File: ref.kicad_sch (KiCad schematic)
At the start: 54 parts, among them Q201 Q_NPN_BCE, U201 Opamp_Dual, U202 ADR1000, U203 ADA4523-1

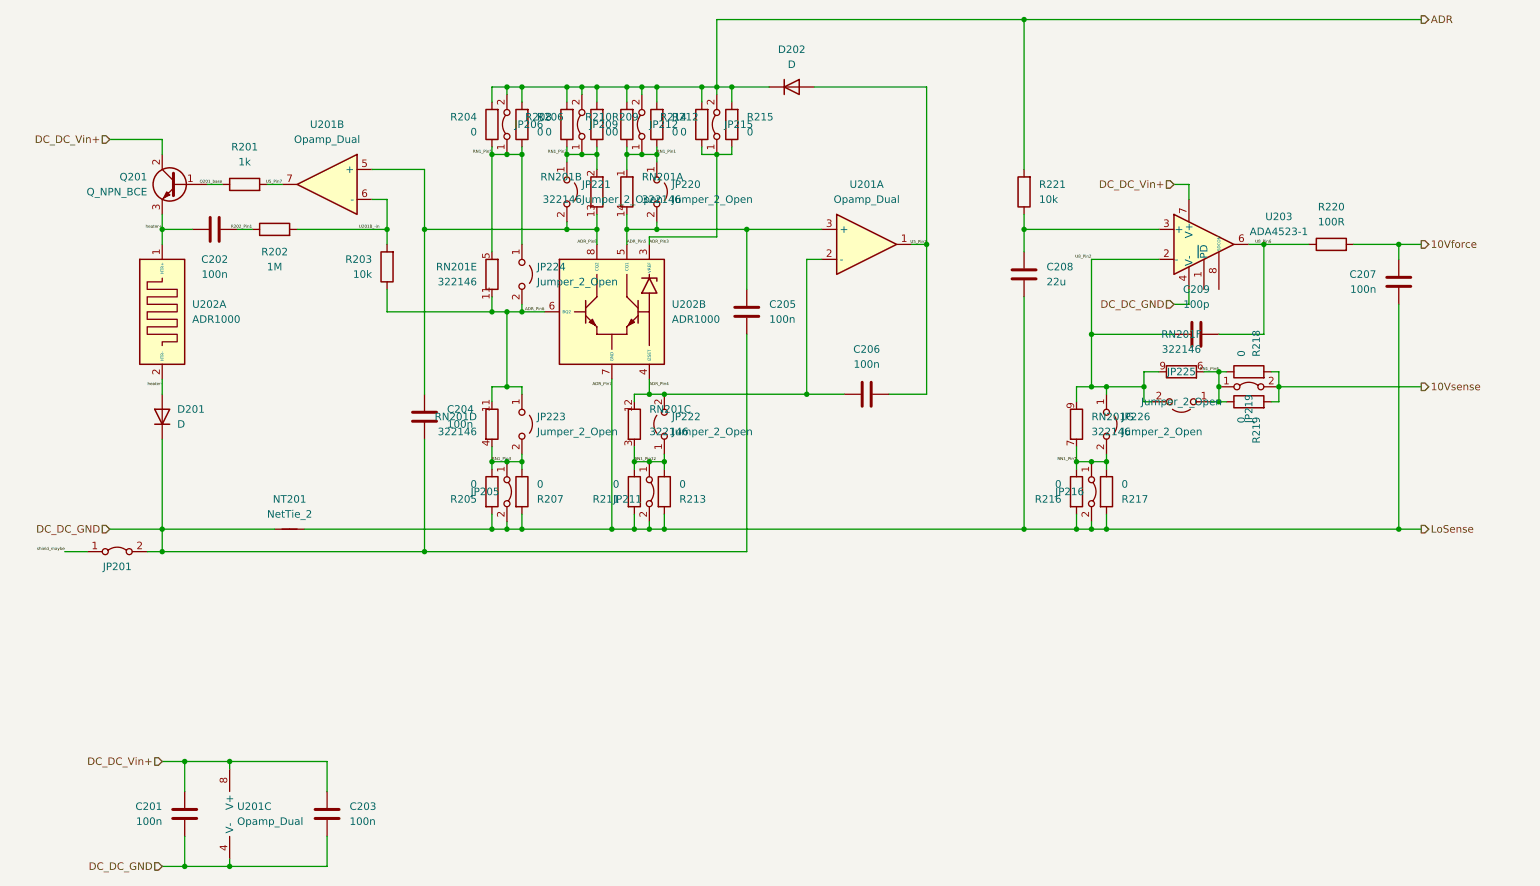
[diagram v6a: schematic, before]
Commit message: schematics updated to rev.2
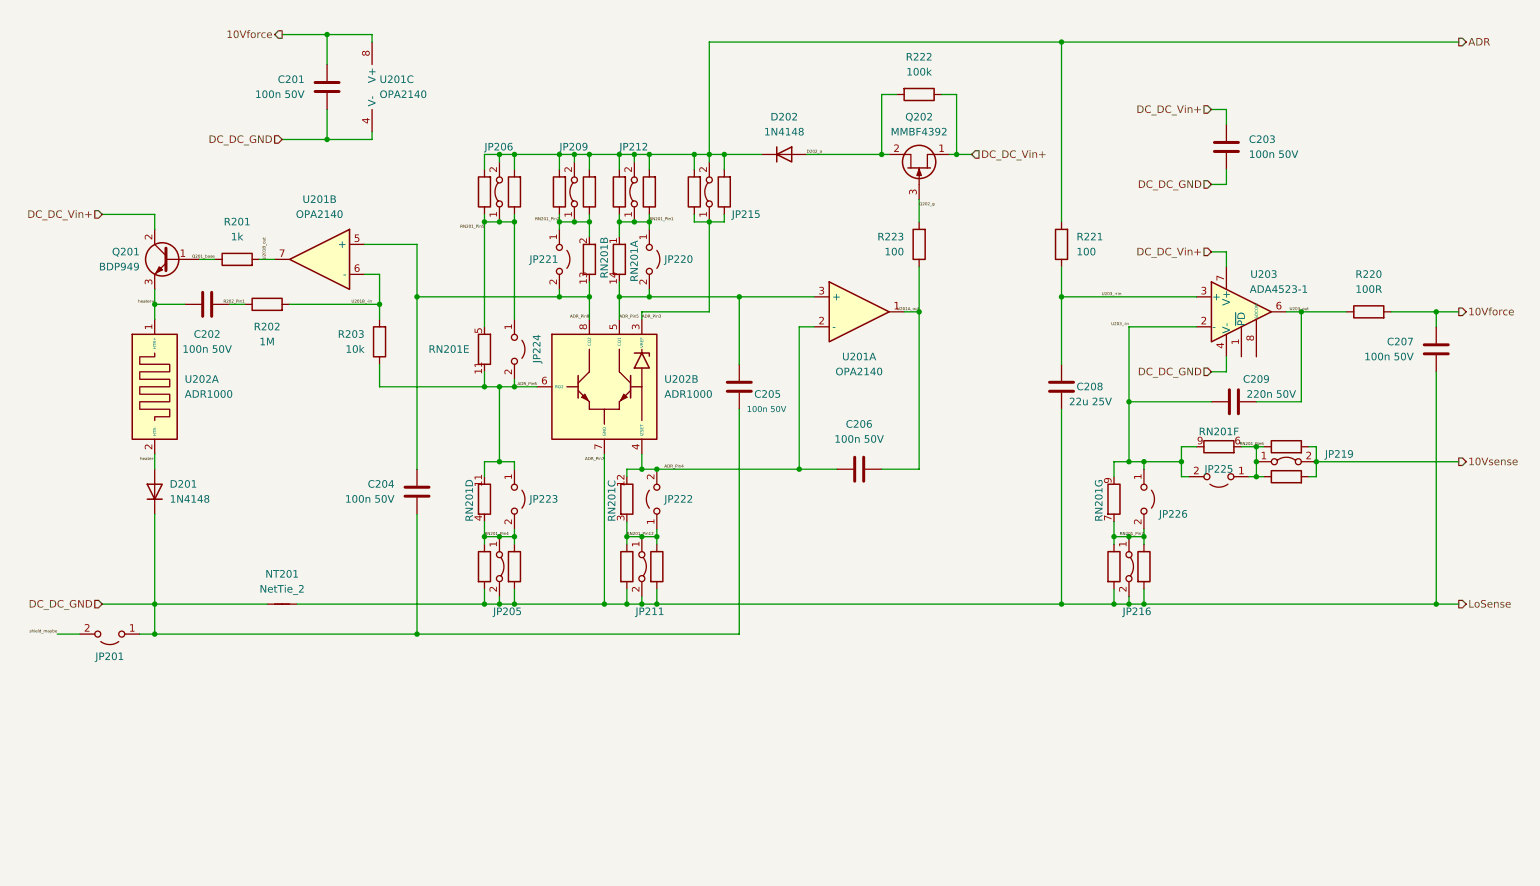
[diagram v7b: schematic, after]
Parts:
- removed JP201: Jumper_2_Bridged, Jumper:SolderJumper-2_P1.3mm_Bridged_RoundedPad1.0x1.5mm, symbol Jumper:Jumper_2_Bridged
- added JP201: Jumper_2_Open, Jumper:SolderJumper-2_P1.3mm_Open_RoundedPad1.0x1.5mm, symbol Jumper:Jumper_2_Open
- added Q202: MMBF4392, Package_TO_SOT_SMD:SOT-23, symbol Transistor_FET:MMBF4392
- added R222: 100k, Resistor_SMD:R_0805_2012Metric, symbol Device:R
- added R223: 100, Resistor_SMD:R_0805_2012Metric, symbol Device:R
- C201, C202, C203, C204, C205, C206, C207: value 100n -> 100n 50V
- C208: value 22u -> 22u 25V
- C209: value 100p -> 220n 50V
- D201, D202: value D -> 1N4148
- JP205, JP206, JP209, JP211, JP212, JP215, JP216, JP219, JP220, JP221, JP222, JP223, JP224, JP225, JP226, R204, R205, R206, R207, R208, R209, R210, R211, R212, R213, R214, R215, R216, R217, R218, R219: now left out of the parts list
- Q201: value Q_NPN_BCE -> BDP949
- R221: value 10k -> 100
- U201: value Opamp_Dual -> OPA2140
- U201: value Opamp_Dual -> OPA2140; footprint (none) -> Package_SO:SOIC-8_3.9x4.9mm_P1.27mm
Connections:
- net 10Vforce: now also C201.2, U201.8 (V+)
- net DC_DC_GND: now also JP201.1 (A)
- net DC_DC_Vin+: now also Q202.1 (D), R222.1; no longer C201.2, U201.8 (V+)
- net shield_maybe: now also JP201.2 (B)
- net U203_+in: now reaches C208.1, R221.1, U203.3 (+)
- net RN1_Pin1 renamed RN201_Pin1
- net RN1_Pin12 renamed RN201_Pin12
- net RN1_Pin2 renamed RN201_Pin2
- net RN1_Pin4 renamed RN201_Pin4
- net RN1_Pin5 renamed RN201_Pin5
- net RN1_Pin6 renamed RN201_Pin6
- net RN1_Pin7 renamed RN201_Pin7
- net U5_Pin1 renamed U201A_out
- net U201A_out: now also R223.1; no longer D202.2 (A)
- net U5_Pin7 renamed U201B_out
- net U8_Pin2 renamed U203_-in
- net U8_Pin6 renamed U203_out
- new net D202_a: D202.2 (A), Q202.2 (S), R222.2
- new net Q202_g: Q202.3 (G), R223.2
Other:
- company: (none) -> RPG
- title: (none) -> Reference and 10V buffer circuit
- moved on the sheet: C201, C202, C203, C204, C205, C206, C207, C208, C209, D201, D202, JP205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

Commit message: asdf
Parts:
- renumbered C202 to C201, C201 to C202, C204 to C203, C205 to C204, C206 to C205, C208 to C206, C203 to C207, C209 to C208, C207 to C209, JP206 to JP202, JP205 to JP203, JP224 to JP204, JP223 to JP205, JP221 to JP206, JP209 to JP207, JP212 to JP208, JP211 to JP209, JP220 to JP210, JP222 to JP211, JP215 to JP212, JP216 to JP213, JP226 to JP214, JP225 to JP215, JP219 to JP216, R222 to R216, R223 to R217, R221 to R218, R216 to R219, R217 to R220, R218 to R221, R219 to R222, R220 to R223, U202 to U201, U201 to U202
